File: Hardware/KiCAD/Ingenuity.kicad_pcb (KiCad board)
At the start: 4 copper layers, 68 x 40.5 mm, 43 parts, among them J1 Conn_01x04, J2 Conn_02x05_Odd_Even, J3 Conn_02x20_Odd_Even, J4 Conn_01x03, J5 Conn_01x03, J8 Conn_ST_STDC14, SW2 SW_Push, U2 STM32L412KBTx, U3 BU33..., U4 LSM6DSM

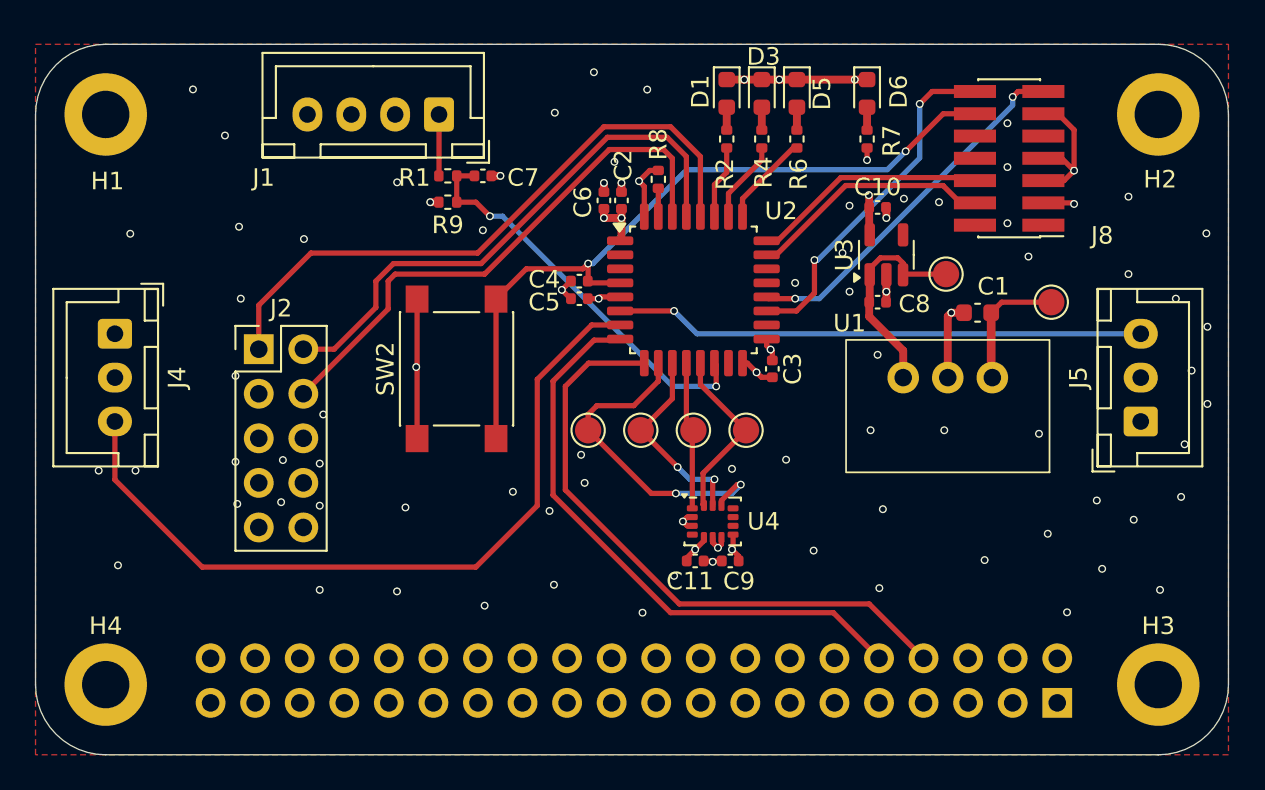
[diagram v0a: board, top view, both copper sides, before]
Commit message: update RasPi connector
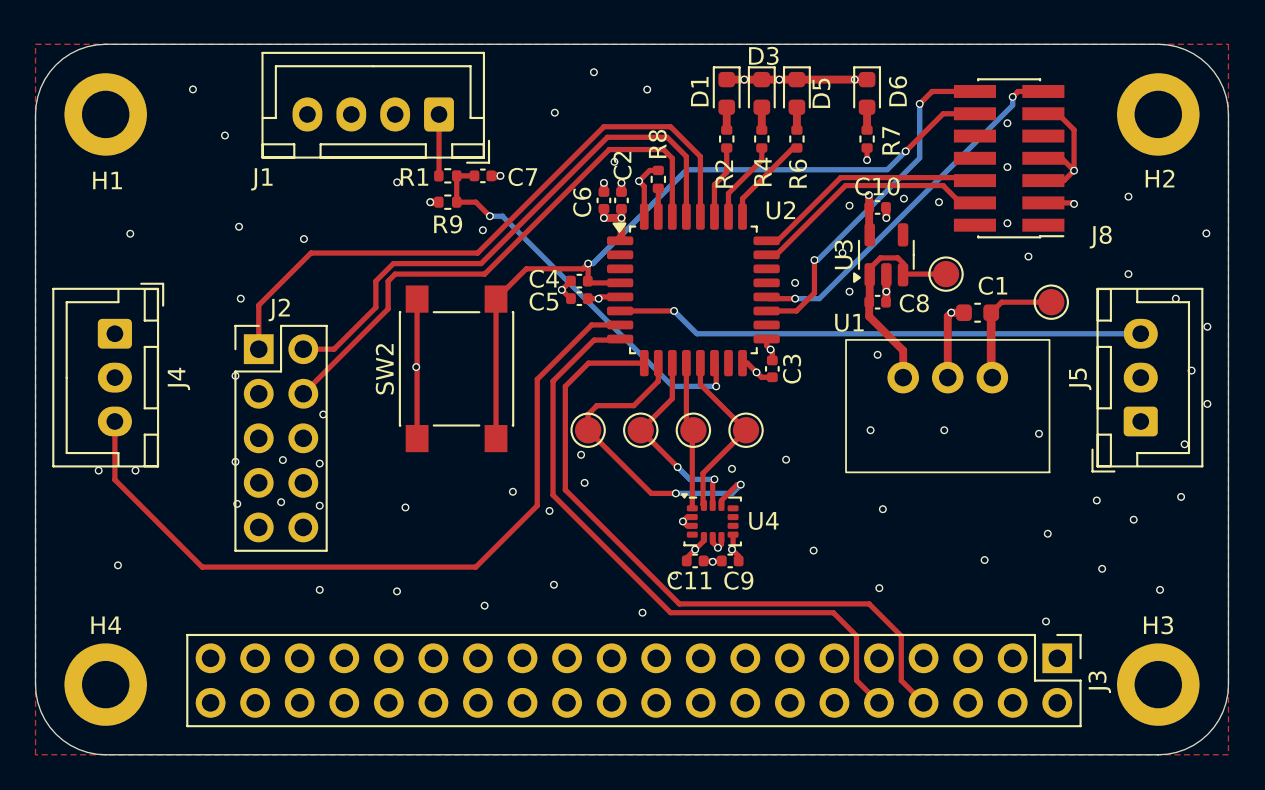
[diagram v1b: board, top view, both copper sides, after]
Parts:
- J3: moved to F.Cu
- moved J3 2.54 mm to (184.7, 126.0), turned to -90 degrees
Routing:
- net +5V: track 33.6 -> 39.6 mm
- net USART2_TX: track 33.8 -> 36.3 mm
- net USART2_RX: track 35.3 -> 37.9 mm

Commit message: update kicad reduction taille pcb
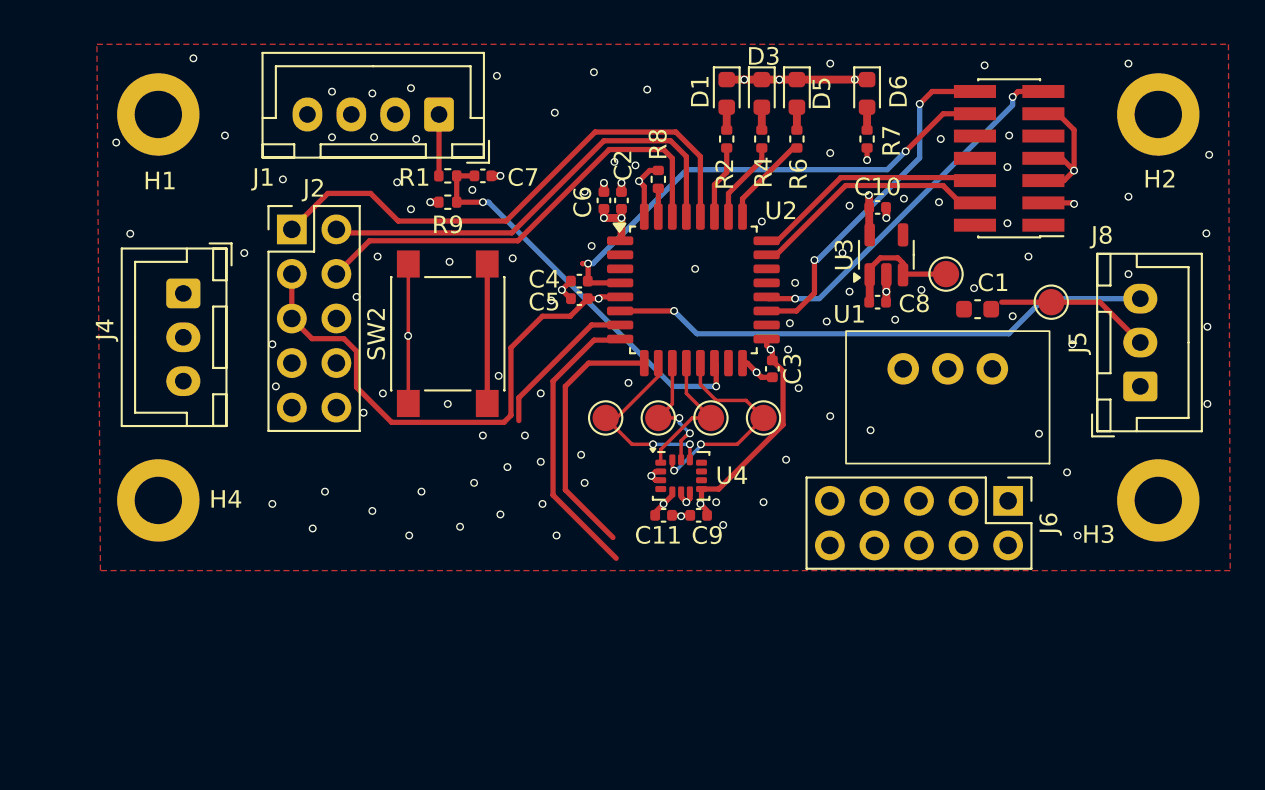
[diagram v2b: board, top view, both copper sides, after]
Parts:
- removed J3: Conn_02x20_Odd_Even, Connector_PinHeader_2.54mm:PinHeader_2x20_P2.54mm_Vertical
- added J6: Conn_02x05_Odd_Even, Connector_PinHeader_2.54mm:PinHeader_2x05_P2.54mm_Vertical, F.Cu at (181.9, 117.0)
- U3: value BU33... -> BU33TD3WG
- moved H4 10.9 mm to (133.5, 117.0)
- moved H3 10.5 mm to (190.5, 117.0)
- moved J2 7.09 mm to (141.1, 101.5)
- moved J4 4.53 mm to (134.9, 105.2)
- moved C11 3.16 mm to (162.3, 117.8)
- moved C9 3.16 mm to (164.3, 117.8)
- moved U4 3.16 mm to (163.3, 115.6)
- moved H1 3.00 mm to (133.5, 95.0)
- moved SW2 2.06 mm to (150.0, 107.5)
- moved J5 2.00 mm to (189.5, 110.5)
- moved TP3 1.22 mm to (159.0, 112.3)
- moved TP4 1.22 mm to (162.0, 112.3)
- moved TP5 1.22 mm to (165.0, 112.3)
- moved TP6 1.22 mm to (168.0, 112.3)
- moved U1 0.50 mm to (178.5, 107.3)
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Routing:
- net +3.3V: track 14.8 -> 52.4 mm
- net PWM2: track 44.1 -> 8.79 mm
- net +5V: track 39.6 -> 7.33 mm
- net USART2_RX: track 37.9 -> 14.8 mm
- net USART2_TX: track 36.3 -> 16.4 mm
- net SPI_CS: track 18.9 -> 11.0 mm
- net +6V: track 15.9 -> 8.94 mm
- net NRST: track 42.5 -> 36.7 mm
- net I2C1_SDA: track 31.3 -> 25.6 mm
- net I2C1_SCL: track 31.6 -> 26.0 mm
- net INT: track 36.0 -> 30.9 mm
- net GND: track 43.9 -> 38.9 mm, vias 87 -> 111
- net SPI1_SCK: track 11.5 -> 7.55 mm
- net SPI1_MOSI: track 10.2 -> 12.7 mm, vias 0 -> 2
- net PWM1: track 30.2 -> 31.0 mm
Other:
- board outline removed

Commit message: end kicad V2
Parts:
- moved C1 1.63 mm to (181.4, 105.0)
- moved U1 0.76 mm to (178.4, 106.6)
- moved TP1 0.70 mm to (184.4, 105.0)
- moved J6 0.62 mm to (181.9, 116.4)
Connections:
- J6 pad 1: unconnected-(J6-Pin_1-Pad1) -> +5V
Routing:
- net +5V: track 7.33 -> 29.1 mm, vias 0 -> 1
- net PWM2: track 8.79 -> 30.0 mm
- net USART2_RX: track 14.8 -> 30.7 mm
- net USART2_TX: track 16.4 -> 29.2 mm
- net +6V: track 8.94 -> 12.8 mm
- net GND: vias 111 -> 142

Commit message: end KiCad V2
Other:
- board outline added: 65 x 30 mm
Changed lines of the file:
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@@
 		)
 	)
+	(gr_line
+		(start 190.5 121)
+		(end 133.5 121)
+		(stroke
+			(width 0.05)
+			(type default)
+		)
+		(layer "Edge.Cuts")
+	)
+	(gr_arc
+		(start 194.5 117)
+		(mid 193.328427 119.828427)
+		(end 190.5 121)
+		(stroke
+			(width 0.05)
+			(type default)
+		)
+		(layer "Edge.Cuts")
+	)
+	(gr_line
+		(start 194.5 95)
+		(end 194.5 117)
+		(stroke
+			(width 0.05)
+			(type default)
+		)
+		(layer "Edge.Cuts")
+	)
+	(gr_arc
+		(start 190.5 91)
+		(mid 193.328427 92.171573)
+		(end 194.5 95)
+		(stroke
+			(width 0.05)
+			(type default)
+		)
+		(layer "Edge.Cuts")
+	)
+	(gr_arc
+		(start 133.5 121)
+		(mid 130.671573 119.828427)
+		(end 129.5 117)
+		(stroke
+			(width 0.05)
+			(type default)
+		)
+		(layer "Edge.Cuts")
+	)
+	(gr_line
+		(start 133.5 91)
+		(end 190.5 91)
+		(stroke
+			(width 0.05)
+			(type default)
+		)
+		(layer "Edge.Cuts")
+	)
+	(gr_arc
+		(start 129.5 95)
+		(mid 130.671573 92.171573)
+		(end 133.5 91)
+		(stroke
+			(width 0.05)
+			(type default)
+		)
+		(layer "Edge.Cuts")
+	)
+	(gr_line
+		(start 129.5 117)
+		(end 129.5 95)
+		(stroke
+			(width 0.05)
+			(type default)
+		)
+		(layer "Edge.Cuts")
+	)
 	(dimension
 		(type aligned)
@@
 		(start 184 115.2)
 		(end 184 116.88)
-		(width 0.2)
+		(width 1)
 		(layer "In2.Cu")
 		(net 2)
@@
 		(start 181.31 114.2)
 		(end 183 114.2)
-		(width 0.2)
+		(width 1)
 		(layer "In2.Cu")
 		(net 2)
@@
 		(start 181.94 118.94)
 		(end 179.4 118.94)
-		(width 0.2)
+		(width 1)
 		(layer "In2.Cu")
 		(net 2)
@@
 		(start 183 114.2)
 		(end 184 115.2)
-		(width 0.2)
+		(width 1)
 		(layer "In2.Cu")
 		(net 2)
@@
 		(start 175.86 108.75)
 		(end 181.31 114.2)
-		(width 0.2)
+		(width 1)
 		(layer "In2.Cu")
 		(net 2)
@@
 		(start 184 116.88)
 		(end 181.94 118.94)
-		(width 0.2)
+		(width 1)
 		(layer "In2.Cu")
 		(net 2)
@@
 		(start 182.175 105)
 		(end 182.175 107.515)
-		(width 0.2)
+		(width 1)
 		(layer "F.Cu")
 		(net 15)
@@
 		(start 182.175 107.515)
 		(end 180.94 108.75)
-		(width 0.2)
+		(width 1)
 		(layer "F.Cu")
 		(net 15)
@@
 		(start 184.4 105)
 		(end 186.475 105)
-		(width 0.2)
+		(width 1)
 		(layer "F.Cu")
 		(net 15)
@@
 		(start 184.4 105)
 		(end 182.175 105)
-		(width 0.2)
+		(width 1)
 		(layer "F.Cu")
 		(net 15)
@@
 		(start 186.475 105)
 		(end 189.475 108)
-		(width 0.2)
+		(width 1)
 		(layer "F.Cu")
 		(net 15)
@@
 	)
 	(via
-		(at 190.6 120.5)
-		(size 0.45)
-		(drill 0.3)
-		(layers "F.Cu" "B.Cu")
-		(free yes)
-		(net 47)
-	)
-	(via
 		(at 188.8 102.5)
 		(size 0.45)
@@
 	)
 	(via
-		(at 130.5 96.8)
+		(at 130.7 96.8)
 		(size 0.45)
 		(drill 0.3)
@@
 	)
 	(via
-		(at 135.5 91.8)
+		(at 135.2 92)
 		(size 0.45)
 		(drill 0.3)
@@
 	)
 	(via
-		(at 178.7 110.5)
+		(at 179.4 110.4)
 		(size 0.45)
 		(drill 0.3)
@@
 	)
 	(via
+		(at 188.6 119.9)
+		(size 0.45)
+		(drill 0.3)
+		(layers "F.Cu" "B.Cu")
+		(free yes)
+		(net 47)
+	)
+	(via
 		(at 163.3 117.9)
 		(size 0.45)
@@
 		(min_thickness 0.25)
 		(filled_areas_thickness no)
-		(fill
+		(fill yes
 			(thermal_gap 0.5)
 			(thermal_bridge_width 0.5)
@@
 		(polygon
 			(pts
-				(xy 129.5 91) (xy 194.5 91) (xy 194.5 121) (xy 129.7 121)
+				(xy 129.5 91) (xy 194.5 91) (xy 194.5 121) (xy 129.5 121)
 			)
 		)
@@
 		(polygon
 			(pts
-				(xy 129.5 91) (xy 194.5 91) (xy 194.5 121) (xy 129.6 121)
+				(xy 129.5 91) (xy 194.5 91) (xy 194.5 121) (xy 129.5 121)
 			)
 		)

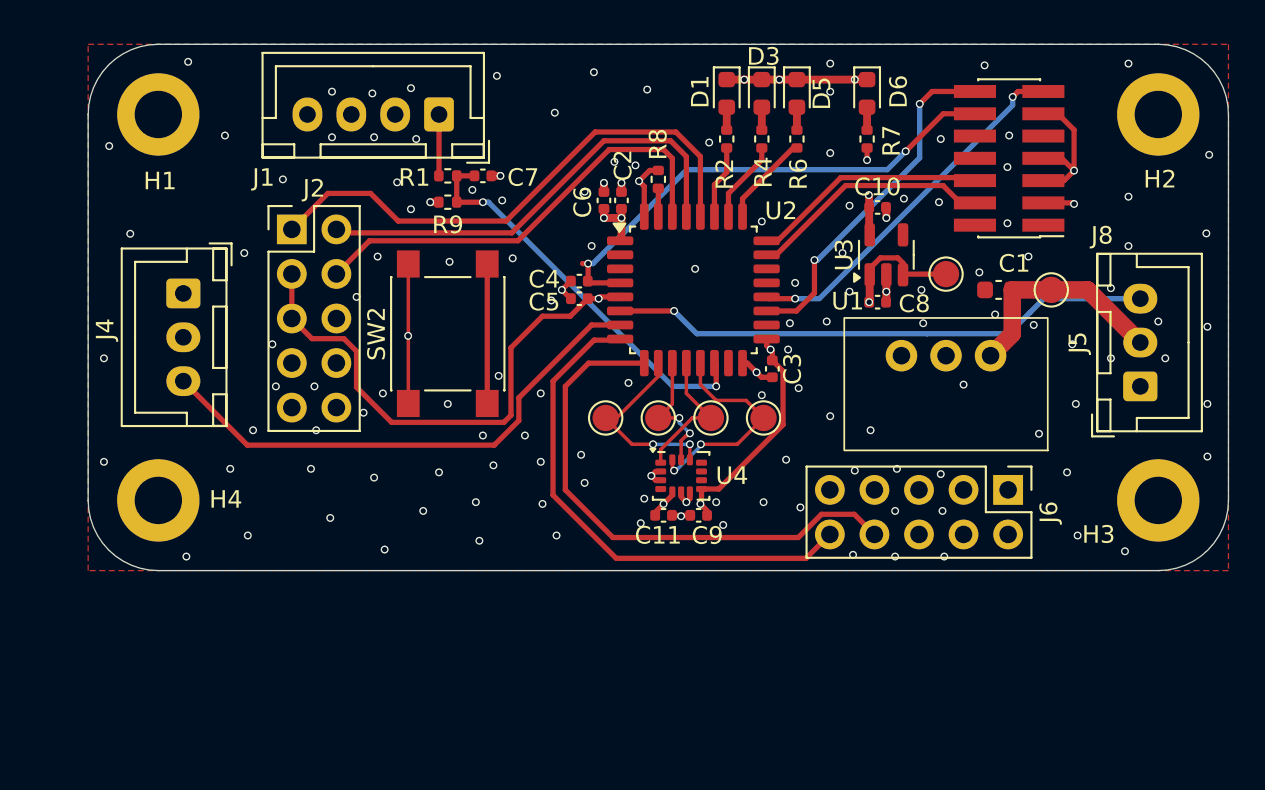
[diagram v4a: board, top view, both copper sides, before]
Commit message: change pcb dimensions and fix errors, ready for fab
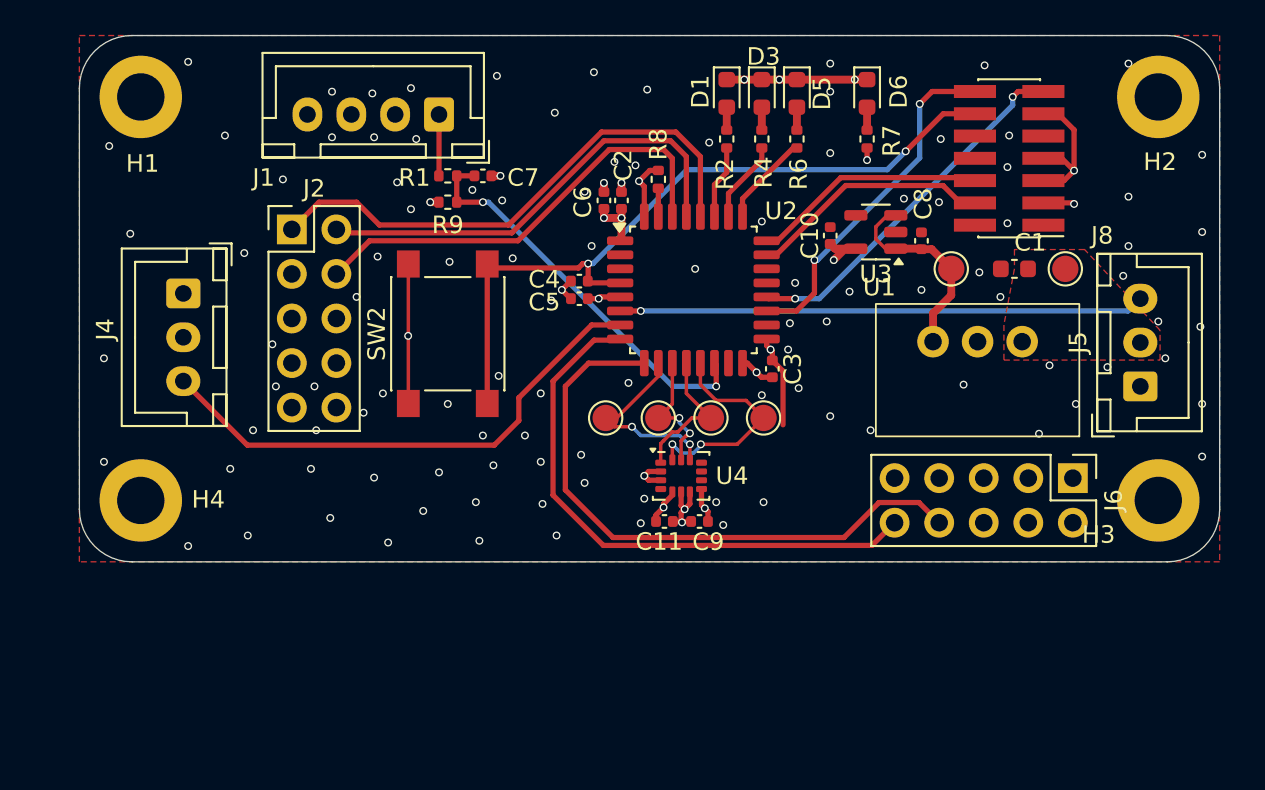
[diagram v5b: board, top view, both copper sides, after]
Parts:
- moved C8 4.30 mm to (177.0, 102.2), turned to 90 degrees
- moved J6 3.75 mm to (185.6, 115.7)
- moved C10 3.14 mm to (171.8, 101.9), turned to 90 degrees
- moved U1 1.97 mm to (180.2, 105.8)
- moved C1 1.50 mm to (182.3, 103.8)
- moved TP1 1.44 mm to (185.2, 103.8)
- moved U3 1.43 mm to (174.4, 101.7), turned to 180 degrees
- moved H1 1.41 mm to (132.5, 94.0)
- moved H2 1.00 mm to (190.5, 94.0)
- moved H4 1.00 mm to (132.5, 117.0)
- moved TP2 0.42 mm to (178.7, 103.8)
- moved C11 0.35 mm to (162.3, 118.2)
- moved C9 0.35 mm to (164.3, 118.2)
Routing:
- net +3.3V: track 52.4 -> 20.0 mm
- net +5V: track 29.1 -> 11.7 mm, vias 1 -> 0
- net +6V: track 12.8 -> 0.00 mm
- net NRST: track 36.7 -> 42.4 mm
- net USART2_RX: track 30.7 -> 34.7 mm
- net USART2_TX: track 29.2 -> 32.5 mm
- net PWM1: track 31.0 -> 29.9 mm
- net GND: track 38.9 -> 39.2 mm, vias 142 -> 122
- added copper zone on In2.Cu, net +5V
- added copper zone on F.Cu, net +6V
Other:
- outline, holes or cut-outs redrawn
